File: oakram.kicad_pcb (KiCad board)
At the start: 2 copper layers, 42.5 x 54 mm, 11 parts, among them U1 IS41C16105C, U2 IS41C16105C, X1 ZIP40, X2 ZIP40

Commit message: oakramv2.zip from https://stardot.org.uk/forums/viewtopic.php?f=16&t=11214&p=193124#p193117
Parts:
- added ?: VIA-0.6mm, VIA-0.6mm, F.Cu at (148.3, 77.7)
- added ?: VIA-0.6mm, VIA-0.6mm, F.Cu at (140.1, 77.7)
- added ?: VIA-0.6mm, VIA-0.6mm, F.Cu at (144.4, 77.7)
- added ? (x2): VIA-0.6mm, VIA-0.6mm, F.Cu at (132.3, 77.7)
- added ? (x2): VIA-0.6mm, VIA-0.6mm, F.Cu at (136.3, 77.7)
- added ?: VIA-0.6mm, VIA-0.6mm, F.Cu at (147.8, 123.3)
- added ?: VIA-0.6mm, VIA-0.6mm, F.Cu at (134.0, 123.2)
- moved X2 0.38 mm to (157.7, 100.3)
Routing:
- net VSS: track 95.9 -> 2.17 mm, vias 29 -> 3
- net VCC: track 63.7 -> 12.6 mm, vias 9 -> 12
- net /~OE: track 57.7 -> 64.0 mm
- net /D25: track 29.7 -> 25.2 mm
- net /D27: track 29.1 -> 25.4 mm
- net /D24: track 24.4 -> 22.0 mm
- net /D15: track 26.0 -> 28.2 mm
- net /A7: track 30.8 -> 33.0 mm
- net /A6: track 30.8 -> 33.0 mm
- net /A8: track 36.4 -> 38.5 mm
- net /D14: track 23.2 -> 25.2 mm
- net /D26: track 24.4 -> 22.6 mm
- net /D13: track 26.0 -> 27.7 mm
- net /A4: track 25.1 -> 26.5 mm
- net /~CAS1: track 28.8 -> 30.0 mm
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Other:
- board text added: "tnt2017 dj2018"
- board text removed: "tnt23 2017"

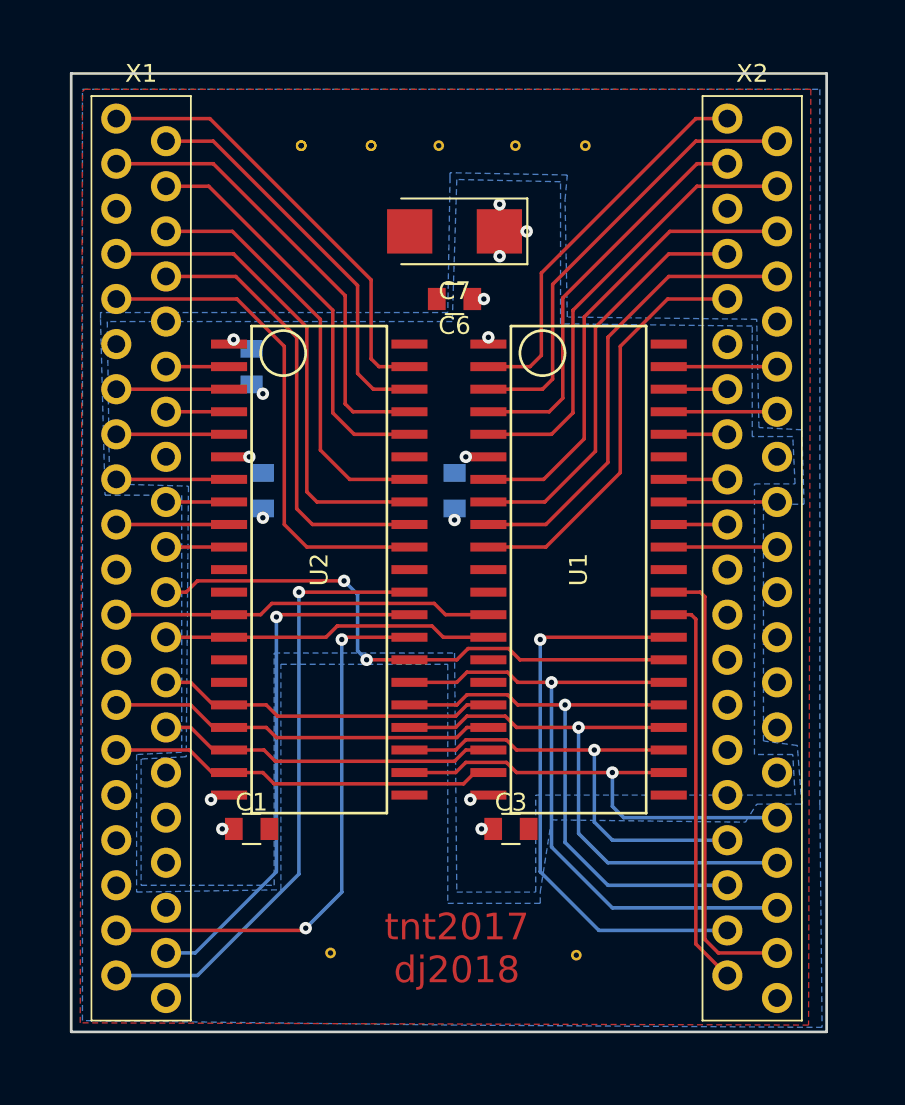
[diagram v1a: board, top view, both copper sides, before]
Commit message: oakramv2.zip from https://stardot.org.uk/forums/viewtopic.php?f=16&t=11214&p=193124#p193124
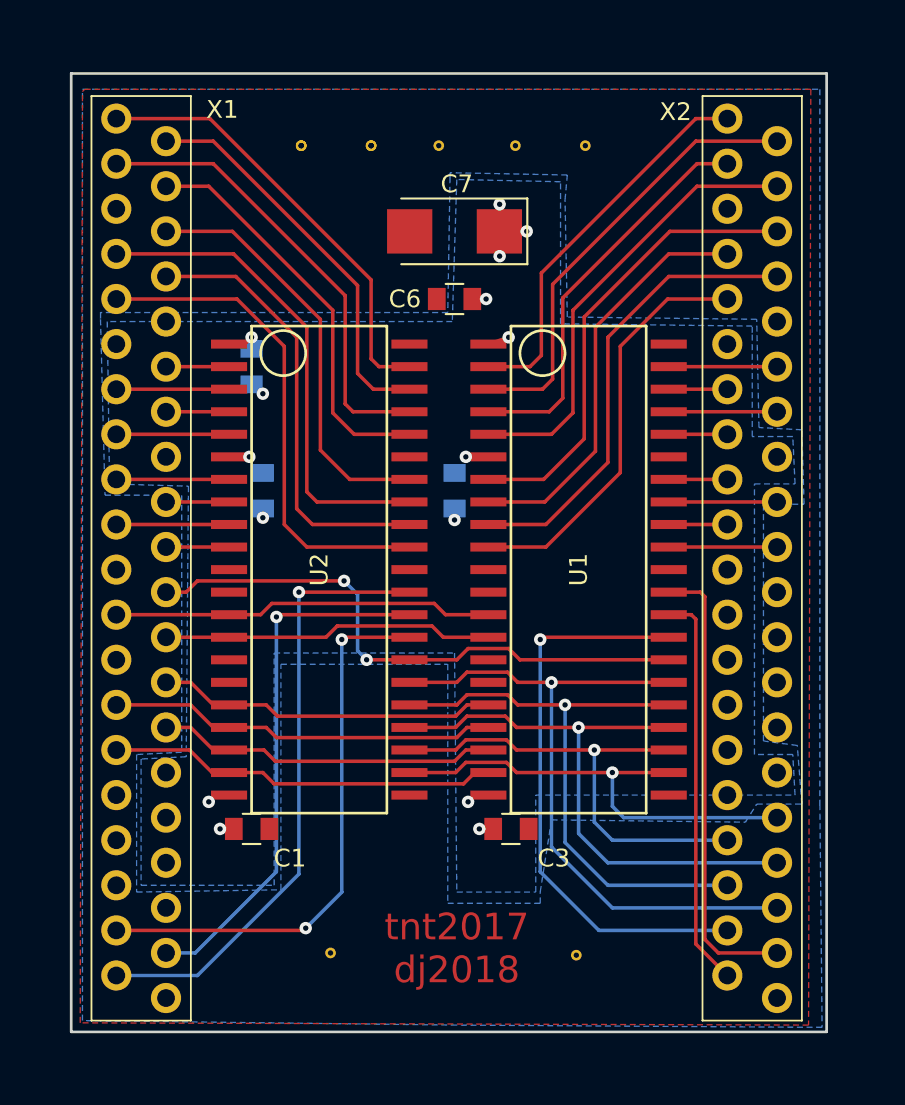
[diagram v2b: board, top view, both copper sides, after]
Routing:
- net VCC: track 12.6 -> 15.5 mm
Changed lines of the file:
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@@
     (links 108)
     (no_connects 1)
-    (area 119.304999 72.885 178.665 136.050001)
+    (area 119.304999 73.584999 178.665 136.050001)
     (thickness 1.6)
     (drawings 9)
-    (tracks 276)
+    (tracks 277)
     (zones 0)
     (modules 20)
@@
   (page A4)
   (layers
-    (0 F.Cu signal)
-    (31 B.Cu signal)
+    (0 F.Cu signal hide)
+    (31 B.Cu signal hide)
     (32 B.Adhes user)
-    (33 F.Adhes user)
+    (33 F.Adhes user hide)
     (34 B.Paste user)
     (35 F.Paste user)
@@
     (37 F.SilkS user)
     (38 B.Mask user hide)
-    (39 F.Mask user hide)
+    (39 F.Mask user)
     (40 Dwgs.User user)
     (41 Cmts.User user)
@@
     (visible_elements 7FFFFFFF)
     (pcbplotparams
-      (layerselection 0x00030_ffffffff)
+      (layerselection 0x010f0_80000001)
       (usegerberextensions false)
       (usegerberattributes true)
@@
       (outputformat 1)
       (mirror false)
-      (drillshape 1)
+      (drillshape 0)
       (scaleselection 1)
-      (outputdirectory ""))
+      (outputdirectory gerbers))
   )
   (net 0 "")
@@
   (module oakram:ZIP40-P-475-1.27 (layer F.Cu)
     (at 123.32 100.33)
-    (fp_text reference X1 (at 0 -26.67) (layer F.SilkS)
+    (fp_text reference X1 (at 4.569 -24.638) (layer F.SilkS)
       (effects (font (size 1 1) (thickness 0.15)))
     )
@@
   (module oakram:ZIP40-P-475-1.27 (layer F.Cu)
     (at 157.734 100.33)
-    (fp_text reference X2 (at 0 -26.67) (layer F.SilkS)
+    (fp_text reference X2 (at -4.318 -24.511) (layer F.SilkS)
       (effects (font (size 1 1) (thickness 0.15)))
     )
@@
     (tags "capacitor 0805")
     (attr smd)
-    (fp_text reference C1 (at 0 -1.5) (layer F.SilkS)
+    (fp_text reference C1 (at 2.159 1.651) (layer F.SilkS)
       (effects (font (size 1 1) (thickness 0.15)))
     )
@@
     (tags "capacitor 0805")
     (attr smd)
-    (fp_text reference C3 (at 0 -1.5) (layer F.SilkS)
+    (fp_text reference C3 (at 2.413 1.651) (layer F.SilkS)
       (effects (font (size 1 1) (thickness 0.15)))
     )
@@
     (tags "capacitor 0805")
     (attr smd)
-    (fp_text reference C6 (at 0 -1.5 180) (layer F.SilkS)
+    (fp_text reference C6 (at 2.794 0 180) (layer F.SilkS)
       (effects (font (size 1 1) (thickness 0.15)))
     )
@@
     (tags "capacitor tantalum smd")
     (attr smd)
-    (fp_text reference C7 (at 0 -3.35 180) (layer F.SilkS)
+    (fp_text reference C7 (at -0.127 2.667 180) (layer F.SilkS)
       (effects (font (size 1 1) (thickness 0.15)))
     )
@@
   (via (at 130.175 91.694) (size 0.7) (drill 0.3) (layers F.Cu B.Cu) (net 56))
   (segment (start 129.54 91.17) (end 129.54 91.313) (width 0.2) (layer B.Cu) (net 56))
+  (segment (start 128.27 88.9) (end 129.159 88.9) (width 0.2) (layer F.Cu) (net 57))
+  (segment (start 129.159 88.9) (end 129.54 88.519) (width 0.2) (layer F.Cu) (net 57))
+  (via (at 129.54 88.519) (size 0.7) (drill 0.3) (layers F.Cu B.Cu) (net 57))
+  (segment (start 129.54 88.519) (end 129.54 89.17) (width 0.2) (layer B.Cu) (net 57))
   (segment (start 128.27 114.3) (end 127.508 114.3) (width 0.2) (layer F.Cu) (net 57))
-  (segment (start 127.508 114.3) (end 127.254 114.554) (width 0.2) (layer F.Cu) (net 57))
-  (via (at 127.254 114.554) (size 0.7) (drill 0.3) (layers F.Cu B.Cu) (net 57))
+  (segment (start 127.508 114.3) (end 127.127 114.681) (width 0.2) (layer F.Cu) (net 57))
+  (via (at 127.127 114.681) (size 0.7) (drill 0.3) (layers F.Cu B.Cu) (net 57))
   (segment (start 142.875 114.3) (end 142.113 114.3) (width 0.2) (layer F.Cu) (net 57))
-  (segment (start 142.113 114.3) (end 141.859 114.554) (width 0.2) (layer F.Cu) (net 57))
-  (via (at 141.859 114.554) (size 0.7) (drill 0.3) (layers F.Cu B.Cu) (net 57))
-  (segment (start 143.145 116.205) (end 142.494 116.205) (width 0.2) (layer F.Cu) (net 57))
-  (via (at 142.494 116.205) (size 0.7) (drill 0.3) (layers F.Cu B.Cu) (net 57))
-  (segment (start 128.54 116.205) (end 127.889 116.205) (width 0.2) (layer F.Cu) (net 57))
-  (via (at 127.889 116.205) (size 0.7) (drill 0.3) (layers F.Cu B.Cu) (net 57))
-  (segment (start 128.27 88.9) (end 128.524 88.646) (width 0.2) (layer F.Cu) (net 57))
-  (via (at 128.524 88.646) (size 0.7) (drill 0.3) (layers F.Cu B.Cu) (net 57))
-  (segment (start 128.27 88.9) (end 128.651 88.9) (width 0.2) (layer F.Cu) (net 57))
+  (segment (start 142.113 114.3) (end 141.732 114.681) (width 0.2) (layer F.Cu) (net 57))
+  (via (at 141.732 114.681) (size 0.7) (drill 0.3) (layers F.Cu B.Cu) (net 57))
+  (segment (start 143.145 116.205) (end 142.367 116.205) (width 0.2) (layer F.Cu) (net 57))
+  (via (at 142.367 116.205) (size 0.7) (drill 0.3) (layers F.Cu B.Cu) (net 57))
+  (segment (start 128.54 116.205) (end 127.762 116.205) (width 0.2) (layer F.Cu) (net 57))
+  (via (at 127.762 116.205) (size 0.7) (drill 0.3) (layers F.Cu B.Cu) (net 57))
   (segment (start 142.875 95.25) (end 141.605 95.25) (width 0.2) (layer F.Cu) (net 57))
   (via (at 141.605 95.25) (size 0.7) (drill 0.3) (layers F.Cu B.Cu) (net 57))
@@
   (via (at 129.413 95.25) (size 0.7) (drill 0.3) (layers F.Cu B.Cu) (net 57))
   (segment (start 129.54 89.17) (end 129.54 88.773) (width 0.2) (layer B.Cu) (net 57))
-  (segment (start 141.97 86.36) (end 142.621 86.36) (width 0.2) (layer F.Cu) (net 57))
-  (via (at 142.621 86.36) (size 0.7) (drill 0.3) (layers F.Cu B.Cu) (net 57))
-  (segment (start 142.875 88.9) (end 142.875 88.519) (width 0.2) (layer F.Cu) (net 57))
-  (via (at 142.875 88.519) (size 0.7) (drill 0.3) (layers F.Cu B.Cu) (net 57))
+  (segment (start 141.97 86.36) (end 142.748 86.36) (width 0.2) (layer F.Cu) (net 57))
+  (via (at 142.748 86.36) (size 0.7) (drill 0.3) (layers F.Cu B.Cu) (net 57))
+  (segment (start 142.875 88.9) (end 144.018 88.519) (width 0.2) (layer F.Cu) (net 57))
+  (via (at 144.018 88.519) (size 0.7) (drill 0.3) (layers F.Cu B.Cu) (net 57))
   (segment (start 143.495 82.55) (end 143.495 83.932) (width 0.2) (layer F.Cu) (net 57))
   (via (at 143.51 83.947) (size 0.7) (drill 0.3) (layers F.Cu B.Cu) (net 57))
@@
   (via (at 143.51 81.026) (size 0.7) (drill 0.3) (layers F.Cu B.Cu) (net 57))
   (segment (start 143.495 81.041) (end 143.51 81.026) (width 0.2) (layer F.Cu) (net 57))
-  (zone (net 0) (net_name "") (layer F.Mask) (hatch full 0.508)
-    (connect_pads (clearance 0.254))
-    (min_thickness 0.254)
-    (fill yes (arc_segments 16) (thermal_gap 0.508) (thermal_bridge_width 0.508))
-    (polygon
-      (pts
-        (xy 134.366 120.65) (xy 147.574 120.65) (xy 147.574 123.444) (xy 134.366 123.444)
-      )
-    )
-  )
   (zone (net 56) (net_name VSS) (layer F.Cu) (hatch edge 0.508)
     (connect_pads (clearance 0.254))
     (min_thickness 0.127)
-    (fill yes (arc_segments 16) (thermal_gap 0.254) (thermal_bridge_width 0.254))
+    (fill yes (arc_segments 16) (thermal_gap 0.254) (thermal_bridge_width 0.508))
     (polygon
       (pts
@@
     (connect_pads (clearance 0.254))
     (min_thickness 0.127)
-    (fill yes (arc_segments 16) (thermal_gap 0.254) (thermal_bridge_width 0.254))
+    (fill yes (arc_segments 16) (thermal_gap 0.254) (thermal_bridge_width 0.508))
     (polygon
       (pts
@@
     (connect_pads (clearance 0.254))
     (min_thickness 0.127)
-    (fill yes (arc_segments 16) (thermal_gap 0.254) (thermal_bridge_width 0.254))
+    (fill yes (arc_segments 16) (thermal_gap 0.254) (thermal_bridge_width 0.508))
     (polygon
       (pts
@@
       )
     )
+  )
+  (zone (net 0) (net_name "") (layer F.Mask) (hatch edge 0.508)
+    (connect_pads (clearance 0.254))
+    (min_thickness 0.127)
+    (fill yes (arc_segments 16) (thermal_gap 0.254) (thermal_bridge_width 0.508))
+    (polygon
+      (pts
+        (xy 136.525 120.396) (xy 145.542 120.396) (xy 145.542 125.73) (xy 136.525 125.73)
+      )
+    )

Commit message: oakramv2.zip from https://stardot.org.uk/forums/viewtopic.php?f=16&t=11214&p=193124#p193131
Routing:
- net VCC: track 15.5 -> 12.6 mm
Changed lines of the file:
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@@
-(kicad_pcb (version 4) (host pcbnew 4.0.7)
+(kicad_pcb (version 20171130) (host pcbnew no-vcs-found-3ad3869~61~ubuntu17.10.1)
   (general
-    (links 108)
-    (no_connects 1)
-    (area 119.304999 73.584999 178.665 136.050001)
     (thickness 1.6)
     (drawings 9)
-    (tracks 277)
+    (tracks 276)
     (zones 0)
     (modules 20)
@@
   (page A4)
   (layers
-    (0 F.Cu signal hide)
-    (31 B.Cu signal hide)
+    (0 F.Cu signal)
+    (31 B.Cu signal)
     (32 B.Adhes user)
-    (33 F.Adhes user hide)
+    (33 F.Adhes user)
     (34 B.Paste user)
     (35 F.Paste user)
     (36 B.SilkS user)
     (37 F.SilkS user)
-    (38 B.Mask user hide)
+    (38 B.Mask user)
     (39 F.Mask user)
     (40 Dwgs.User user)
@@
   )
   (setup
-    (last_trace_width 0.2)
+    (last_trace_width 0.25)
     (user_trace_width 0.2)
     (user_trace_width 0.3)
@@
     (visible_elements 7FFFFFFF)
     (pcbplotparams
-      (layerselection 0x010f0_80000001)
+      (layerselection 0x00030_ffffffff)
       (usegerberextensions false)
       (usegerberattributes true)
+      (usegerberadvancedattributes false)
+      (creategerberjobfile false)
       (excludeedgelayer true)
       (linewidth 0.100000)
@@
       (hpglpenspeed 20)
       (hpglpendiameter 15)
-      (hpglpenoverlay 2)
       (psnegative false)
       (psa4output false)
@@
       (outputformat 1)
       (mirror false)
-      (drillshape 0)
+      (drillshape 1)
       (scaleselection 1)
-      (outputdirectory gerbers))
+      (outputdirectory ""))
   )
   (net 0 "")
@@
   (module oakram:ZIP40-P-475-1.27 (layer F.Cu)
     (at 123.32 100.33)
-    (fp_text reference X1 (at 4.569 -24.638) (layer F.SilkS)
+    (fp_text reference X1 (at 4.188 -24.638) (layer F.SilkS)
       (effects (font (size 1 1) (thickness 0.15)))
     )
@@
   (module oakram:ZIP40-P-475-1.27 (layer F.Cu)
     (at 157.734 100.33)
-    (fp_text reference X2 (at -4.318 -24.511) (layer F.SilkS)
+    (fp_text reference X2 (at -4.318 -24.638) (layer F.SilkS)
       (effects (font (size 1 1) (thickness 0.15)))
     )
@@
     (tags "capacitor 0805")
     (attr smd)
-    (fp_text reference C1 (at 2.159 1.651) (layer F.SilkS)
+    (fp_text reference C1 (at 0 1.651) (layer F.SilkS)
       (effects (font (size 1 1) (thickness 0.15)))
     )
@@
     (tags "capacitor 0805")
     (attr smd)
-    (fp_text reference C3 (at 2.413 1.651) (layer F.SilkS)
+    (fp_text reference C3 (at -0.127 1.651) (layer F.SilkS)
       (effects (font (size 1 1) (thickness 0.15)))
     )
@@
     (tags "capacitor tantalum smd")
     (attr smd)
-    (fp_text reference C7 (at -0.127 2.667 180) (layer F.SilkS)
+    (fp_text reference C7 (at 0 2.794 180) (layer F.SilkS)
       (effects (font (size 1 1) (thickness 0.15)))
     )
@@
   (via (at 130.175 91.694) (size 0.7) (drill 0.3) (layers F.Cu B.Cu) (net 56))
   (segment (start 129.54 91.17) (end 129.54 91.313) (width 0.2) (layer B.Cu) (net 56))
-  (segment (start 128.27 88.9) (end 129.159 88.9) (width 0.2) (layer F.Cu) (net 57))
-  (segment (start 129.159 88.9) (end 129.54 88.519) (width 0.2) (layer F.Cu) (net 57))
-  (via (at 129.54 88.519) (size 0.7) (drill 0.3) (layers F.Cu B.Cu) (net 57))
-  (segment (start 129.54 88.519) (end 129.54 89.17) (width 0.2) (layer B.Cu) (net 57))
   (segment (start 128.27 114.3) (end 127.508 114.3) (width 0.2) (layer F.Cu) (net 57))
-  (segment (start 127.508 114.3) (end 127.127 114.681) (width 0.2) (layer F.Cu) (net 57))
-  (via (at 127.127 114.681) (size 0.7) (drill 0.3) (layers F.Cu B.Cu) (net 57))
+  (segment (start 127.508 114.3) (end 127.254 114.554) (width 0.2) (layer F.Cu) (net 57))
+  (via (at 127.254 114.554) (size 0.7) (drill 0.3) (layers F.Cu B.Cu) (net 57))
   (segment (start 142.875 114.3) (end 142.113 114.3) (width 0.2) (layer F.Cu) (net 57))
-  (segment (start 142.113 114.3) (end 141.732 114.681) (width 0.2) (layer F.Cu) (net 57))
-  (via (at 141.732 114.681) (size 0.7) (drill 0.3) (layers F.Cu B.Cu) (net 57))
-  (segment (start 143.145 116.205) (end 142.367 116.205) (width 0.2) (layer F.Cu) (net 57))
-  (via (at 142.367 116.205) (size 0.7) (drill 0.3) (layers F.Cu B.Cu) (net 57))
-  (segment (start 128.54 116.205) (end 127.762 116.205) (width 0.2) (layer F.Cu) (net 57))
-  (via (at 127.762 116.205) (size 0.7) (drill 0.3) (layers F.Cu B.Cu) (net 57))
+  (segment (start 142.113 114.3) (end 141.859 114.554) (width 0.2) (layer F.Cu) (net 57))
+  (via (at 141.859 114.554) (size 0.7) (drill 0.3) (layers F.Cu B.Cu) (net 57))
+  (segment (start 143.145 116.205) (end 142.494 116.205) (width 0.2) (layer F.Cu) (net 57))
+  (via (at 142.494 116.205) (size 0.7) (drill 0.3) (layers F.Cu B.Cu) (net 57))
+  (segment (start 128.54 116.205) (end 127.889 116.205) (width 0.2) (layer F.Cu) (net 57))
+  (via (at 127.889 116.205) (size 0.7) (drill 0.3) (layers F.Cu B.Cu) (net 57))
+  (segment (start 128.27 88.9) (end 128.524 88.646) (width 0.2) (layer F.Cu) (net 57))
+  (via (at 128.524 88.646) (size 0.7) (drill 0.3) (layers F.Cu B.Cu) (net 57))
+  (segment (start 128.27 88.9) (end 128.651 88.9) (width 0.2) (layer F.Cu) (net 57))
   (segment (start 142.875 95.25) (end 141.605 95.25) (width 0.2) (layer F.Cu) (net 57))
   (via (at 141.605 95.25) (size 0.7) (drill 0.3) (layers F.Cu B.Cu) (net 57))
@@
   (via (at 129.413 95.25) (size 0.7) (drill 0.3) (layers F.Cu B.Cu) (net 57))
   (segment (start 129.54 89.17) (end 129.54 88.773) (width 0.2) (layer B.Cu) (net 57))
-  (segment (start 141.97 86.36) (end 142.748 86.36) (width 0.2) (layer F.Cu) (net 57))
-  (via (at 142.748 86.36) (size 0.7) (drill 0.3) (layers F.Cu B.Cu) (net 57))
-  (segment (start 142.875 88.9) (end 144.018 88.519) (width 0.2) (layer F.Cu) (net 57))
-  (via (at 144.018 88.519) (size 0.7) (drill 0.3) (layers F.Cu B.Cu) (net 57))
+  (segment (start 141.97 86.36) (end 142.621 86.36) (width 0.2) (layer F.Cu) (net 57))
+  (via (at 142.621 86.36) (size 0.7) (drill 0.3) (layers F.Cu B.Cu) (net 57))
+  (segment (start 142.875 88.9) (end 142.875 88.519) (width 0.2) (layer F.Cu) (net 57))
+  (via (at 142.875 88.519) (size 0.7) (drill 0.3) (layers F.Cu B.Cu) (net 57))
   (segment (start 143.495 82.55) (end 143.495 83.932) (width 0.2) (layer F.Cu) (net 57))
   (via (at 143.51 83.947) (size 0.7) (drill 0.3) (layers F.Cu B.Cu) (net 57))
@@
   (via (at 143.51 81.026) (size 0.7) (drill 0.3) (layers F.Cu B.Cu) (net 57))
   (segment (start 143.495 81.041) (end 143.51 81.026) (width 0.2) (layer F.Cu) (net 57))
+  (zone (net 0) (net_name "") (layer F.Mask) (hatch full 0.508)
+    (connect_pads (clearance 0.254))
+    (min_thickness 0.254)
+    (fill yes (arc_segments 16) (thermal_gap 0.508) (thermal_bridge_width 0.508))
+    (polygon
+      (pts
+        (xy 136.144 120.142) (xy 146.05 120.142) (xy 146.05 125.984) (xy 136.144 125.984)
+      )
+    )
+  )
   (zone (net 56) (net_name VSS) (layer F.Cu) (hatch edge 0.508)
     (connect_pads (clearance 0.254))
     (min_thickness 0.127)
-    (fill yes (arc_segments 16) (thermal_gap 0.254) (thermal_bridge_width 0.508))
+    (fill yes (arc_segments 16) (thermal_gap 0.254) (thermal_bridge_width 0.254))
     (polygon
       (pts
@@
     (connect_pads (clearance 0.254))
     (min_thickness 0.127)
-    (fill yes (arc_segments 16) (thermal_gap 0.254) (thermal_bridge_width 0.508))
+    (fill yes (arc_segments 16) (thermal_gap 0.254) (thermal_bridge_width 0.254))
     (polygon
       (pts
@@
     (connect_pads (clearance 0.254))
     (min_thickness 0.127)
-    (fill yes (arc_segments 16) (thermal_gap 0.254) (thermal_bridge_width 0.508))
+    (fill yes (arc_segments 16) (thermal_gap 0.254) (thermal_bridge_width 0.254))
     (polygon
       (pts
@@
     )
     (polygon
-      (pts        (xy 160.274 111.506) (xy 158.369 111.252) (xy 158.369 97.917) (xy 160.655 97.917) (xy 160.528 93.726)
+      (pts
+        (xy 160.274 111.506) (xy 158.369 111.252) (xy 158.369 97.917) (xy 160.655 97.917) (xy 160.528 93.726)
         (xy 158.115 93.599) (xy 157.988 87.503) (xy 147.32 87.376) (xy 147.193 80.772) (xy 147.32 79.375)
         (xy 140.716 79.248) (xy 140.716 79.502) (xy 140.589 87.122) (xy 121.031 87.122) (xy 121.031 87.503)
@@
       )
     )
-  )
-  (zone (net 0) (net_name "") (layer F.Mask) (hatch edge 0.508)
-    (connect_pads (clearance 0.254))
-    (min_thickness 0.127)
-    (fill yes (arc_segments 16) (thermal_gap 0.254) (thermal_bridge_width 0.508))
-    (polygon
-      (pts
-        (xy 136.525 120.396) (xy 145.542 120.396) (xy 145.542 125.73) (xy 136.525 125.73)
-      )
-    )
